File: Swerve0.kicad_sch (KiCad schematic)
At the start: 2 parts

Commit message: Jonathan's PDH, swerve, and top-level graphics
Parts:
- removed CB1: CircuitBreaker_1P_US, symbol Device:CircuitBreaker_1P_US
- removed F4: Fuse, symbol Device:Fuse

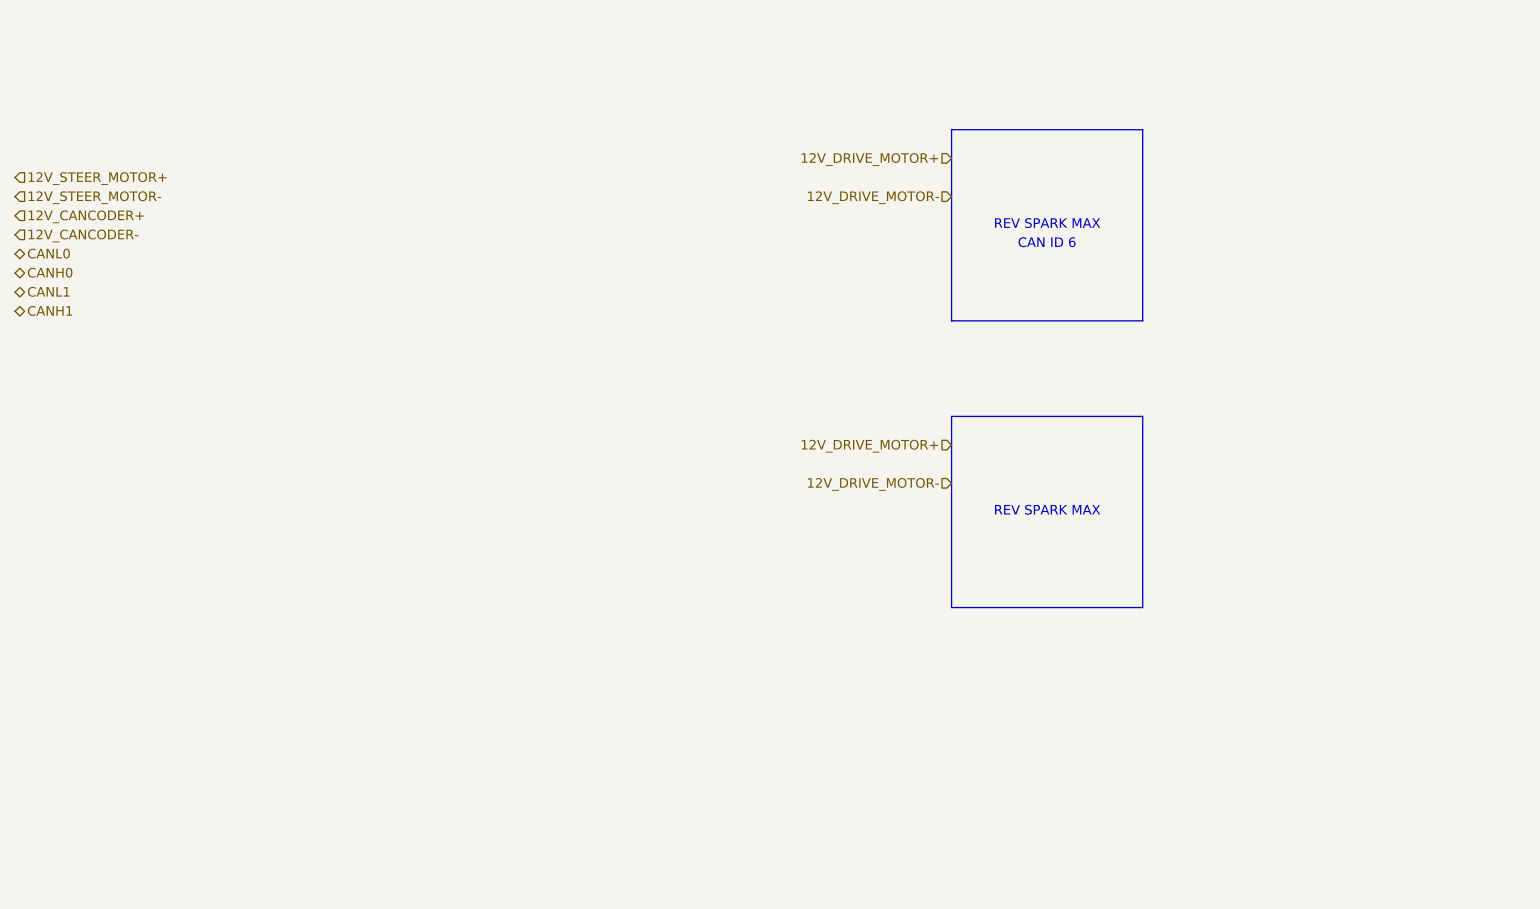
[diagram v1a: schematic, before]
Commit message: Jonathan: Completed roborio, swerve, and top level schematics Added and wired radio
Jeremy:
Fixed unnamed radio file

Signed-off-by: Jeremy Siegfried <jeremy.siegfried@howlandschools.org>
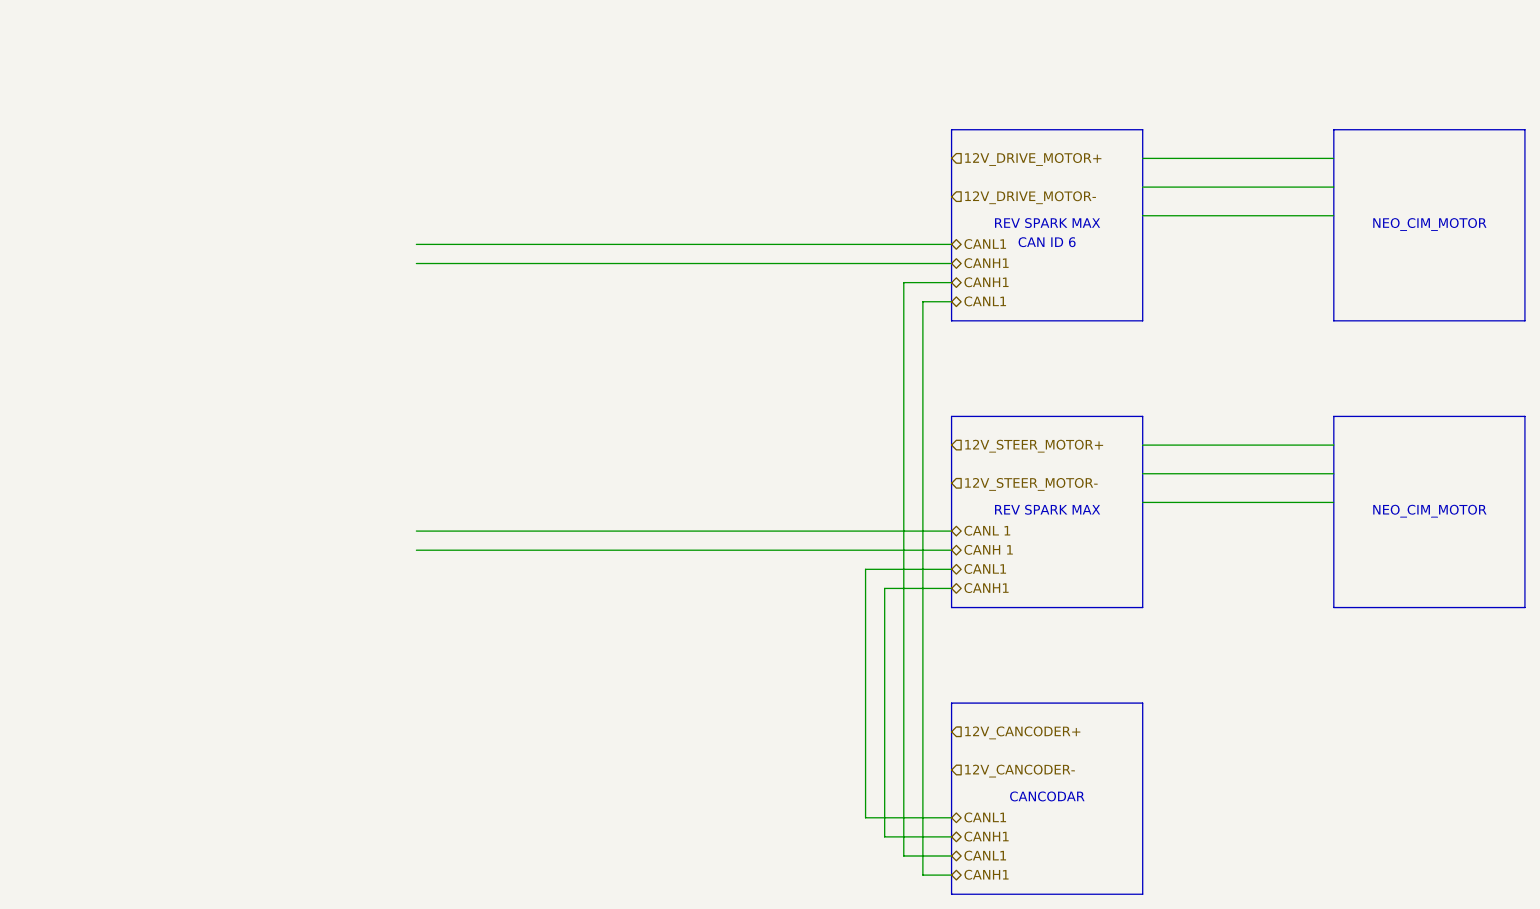
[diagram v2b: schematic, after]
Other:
- note added: "CANCODAR"
- note added: "NEO_CIM_MOTOR"
